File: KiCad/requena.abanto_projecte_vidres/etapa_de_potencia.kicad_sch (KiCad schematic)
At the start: 15 parts, among them U1 L298N, U2 TSR2-2450, U3 MCP6022, U4 LM1117DT-3.3

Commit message: millora_petjades
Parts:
- added FB1: FerriteBead, Inductor_SMD:L_0805_2012Metric, symbol Device:FerriteBead
- added J5: Conn_01x02, TerminalBlock:TerminalBlock_Xinya_XY308-2.54-2P_1x02_P2.54mm_Horizontal, symbol Connector_Generic:Conn_01x02
- added P1, P2: 282837-2, 282837-2:TE_282837-2, symbol 282837-2:282837-2
- C1, C5: footprint (none) -> Capacitor_SMD:C_0805_2012Metric
- C2, C6: footprint (none) -> Capacitor_SMD:C_1206_3216Metric
- C3, C4: footprint (none) -> Capacitor_THT:CP_Radial_D4.0mm_P1.50mm
- D1: footprint (none) -> Diode_THT:D_DO-41_SOD81_P12.70mm_Horizontal
- D2: footprint (none) -> Diode_THT:D_A-405_P2.54mm_Vertical_AnodeUp
- R1: value R_Shunt -> 5m; footprint (none) -> Resistor_SMD:R_1206_3216Metric
- R2: value R -> 1k; footprint (none) -> Resistor_SMD:R_1206_3216Metric
- R3: value R -> 300k; footprint (none) -> Resistor_SMD:R_1206_3216Metric
- U3: footprint (none) -> Package_SO:SOIC-8_3.9x4.9mm_P1.27mm
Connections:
- net +12V: now also J5.2 (Pin_2)
- net AN0: now also U3.6 (-); no longer R3.1, U3.1, U3.5 (+)
- net GND: now also FB1.2; no longer C1.2, C3.2, D2.2 (A), U2.2 (GND), U3.6 (-)
- net at U1.13 (OUT3): now also P2.1
- net at U1.14 (OUT4): now also P2.2
- net at U1.2 (OUT1): now also P1.1
- net at U1.3 (OUT2): now also P1.2
- new net: R3.1, U3.1, U3.5 (+)
- new net GNDPWR: C1.2, C3.2, D2.2 (A), FB1.1, J5.1 (Pin_1), U2.2 (GND)

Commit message: milora_esquema_i_layoutcomençat
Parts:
- P1, P2: footprint 282837-2:TE_282837-2 -> motor_connector:TE_282837-2
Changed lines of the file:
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@@
 			)
 		)
-		(property "Footprint" "282837-2:TE_282837-2"
+		(property "Footprint" "motor_connector:TE_282837-2"
 			(at 148.59 53.34 0)
 			(effects
@@
 			)
 		)
-		(property "Footprint" "282837-2:TE_282837-2"
+		(property "Footprint" "motor_connector:TE_282837-2"
 			(at 148.59 60.96 0)
 			(effects

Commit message: :(
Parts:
- C3: value 1uF -> 470uF
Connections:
- net +12V: no longer D1.2 (A)
- new net V_BAT: D1.2 (A)
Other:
- company: (none) -> AUTORS: ÀLEX REQUENA i ALFRED ABANTO
- title: (none) -> ETAPA DE POTÈNCIA
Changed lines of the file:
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@@
 	(generator_version "9.0")
 	(paper "A4")
+	(title_block
+		(title "ETAPA DE POTÈNCIA")
+		(company "AUTORS: ÀLEX REQUENA i ALFRED ABANTO")
+	)
 	(junction
 		(at 170.18 85.09)
@@
 	)
 	(junction
-		(at 62.23 127)
-		(diameter 0)
-		(color 0 0 0 0)
-	)
-	(junction
 		(at 189.23 143.51)
 		(diameter 0)
@@
 	(wire
 		(pts
-			(xy 62.23 127) (xy 62.23 138.43)
-		)
-		(stroke
-			(width 0)
-			(type default)
-		)
-	)
-	(wire
-		(pts
 			(xy 167.64 143.51) (xy 186.69 143.51)
 		)
@@
 	(wire
 		(pts
-			(xy 62.23 127) (xy 67.31 127)
-		)
-		(stroke
-			(width 0)
-			(type default)
-		)
-	)
-	(wire
-		(pts
 			(xy 208.28 99.06) (xy 208.28 101.6)
 		)
@@
 	(wire
 		(pts
+			(xy 64.77 127) (xy 67.31 127)
+		)
+		(stroke
+			(width 0)
+			(type default)
+		)
+	)
+	(wire
+		(pts
 			(xy 111.76 127) (xy 111.76 133.35)
-		)
-		(stroke
-			(width 0)
-			(type default)
-		)
-	)
-	(wire
-		(pts
-			(xy 62.23 123.19) (xy 62.23 127)
 		)
 		(stroke
@@
 	(global_label "V_BAT"
 		(shape input)
-		(at 62.23 138.43 270)
+		(at 64.77 127 180)
 		(fields_autoplaced yes)
 		(effects
@@
 		)
 		(property "Intersheetrefs" "${INTERSHEET_REFS}"
-			(at 62.23 146.7976 90)
+			(at 56.4024 127 0)
 			(effects
 				(font
@@
 	)
 	(symbol
-		(lib_id "power:+12V")
-		(at 62.23 123.19 0)
-		(unit 1)
-		(exclude_from_sim no)
-		(in_bom yes)
-		(on_board yes)
-		(dnp no)
-		(fields_autoplaced yes)
-		(property "Reference" "#PWR0109"
-			(at 62.23 127 0)
-			(effects
-				(font
-					(size 1.27 1.27)
-				)
-				(hide yes)
-			)
-		)
-		(property "Value" "+12V"
-			(at 62.23 118.11 0)
-			(effects
-				(font
-					(size 1.27 1.27)
-				)
-			)
-		)
-		(property "Footprint" ""
-			(at 62.23 123.19 0)
-			(effects
-				(font
-					(size 1.27 1.27)
-				)
-				(hide yes)
-			)
-		)
-		(property "Datasheet" ""
-			(at 62.23 123.19 0)
-			(effects
-				(font
-					(size 1.27 1.27)
-				)
-				(hide yes)
-			)
-		)
-		(property "Description" "Power symbol creates a global label with name \"+12V\""
-			(at 62.23 123.19 0)
-			(effects
-				(font
-					(size 1.27 1.27)
-				)
-				(hide yes)
-			)
-		)
-		(pin "1"
-		)
-		(instances
-			(project "etapa_de_potencia"
-				(path "/022df46b-4a1f-423b-84a0-dca974b893e8"
-					(reference "#PWR06")
-					(unit 1)
-				)
-			)
-			(project "requena.abanto_projecte_vidres"
-				(path "/4006572a-320d-4ed7-bf52-f860e1c069c6/0b0d2692-6fb2-4ddb-9a32-8981b2e43675"
-					(reference "#PWR0109")
-					(unit 1)
-				)
-			)
-		)
-	)
-	(symbol
 		(lib_id "Device:C")
 		(at 104.14 36.83 90)
@@
 			)
 		)
-		(property "Value" "1uF"
+		(property "Value" "470uF"
 			(at 115.57 137.5409 0)
 			(effects

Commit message: esquema acabat
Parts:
- P1, P2: footprint motor_connector:TE_282837-2 -> 282837-2:TE_282837-2
- R1: value 5m -> 50m; footprint Resistor_SMD:R_1206_3216Metric -> Resistor_SMD:R_Shunt_Vishay_WSK2512_6332Metric_T1.19mm
- R3: value 300k -> 12k
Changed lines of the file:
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@@
 			)
 		)
-		(property "Value" "300k"
+		(property "Value" "12k"
 			(at 163.83 92.71 90)
 			(effects
@@
 			)
 		)
-		(property "Footprint" "motor_connector:TE_282837-2"
+		(property "Footprint" "282837-2:TE_282837-2"
 			(at 148.59 53.34 0)
 			(effects
@@
 			)
 		)
-		(property "Footprint" "motor_connector:TE_282837-2"
+		(property "Footprint" "282837-2:TE_282837-2"
 			(at 148.59 60.96 0)
 			(effects
@@
 			)
 		)
-		(property "Value" "5m"
+		(property "Value" "50m"
 			(at 116.84 88.8999 0)
 			(effects
@@
 			)
 		)
-		(property "Footprint" "Resistor_SMD:R_1206_3216Metric"
+		(property "Footprint" "Resistor_SMD:R_Shunt_Vishay_WSK2512_6332Metric_T1.19mm"
 			(at 117.602 87.63 90)
 			(effects

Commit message: primera pcb
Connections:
- net +12V: no longer J5.2 (Pin_2)
- net V_BAT: now also J5.2 (Pin_2)
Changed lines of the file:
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@@
 	(wire
 		(pts
-			(xy 31.75 96.52) (xy 33.02 96.52)
+			(xy 31.75 96.52) (xy 35.56 96.52)
 		)
 		(stroke
@@
 		(property "Intersheetrefs" "${INTERSHEET_REFS}"
 			(at 208.28 73.3962 90)
+			(effects
+				(font
+					(size 1.27 1.27)
+				)
+				(justify left)
+				(hide yes)
+			)
+		)
+	)
+	(global_label "V_BAT"
+		(shape input)
+		(at 35.56 96.52 90)
+		(fields_autoplaced yes)
+		(effects
+			(font
+				(size 1.27 1.27)
+			)
+			(justify left)
+		)
+		(property "Intersheetrefs" "${INTERSHEET_REFS}"
+			(at 35.56 88.1524 90)
 			(effects
 				(font
@@
 					(unit 1)
 				)
-			)
-		)
-	)
-	(symbol
-		(lib_id "power:+12V")
-		(at 33.02 96.52 0)
-		(unit 1)
-		(exclude_from_sim no)
-		(in_bom yes)
-		(on_board yes)
-		(dnp no)
-		(fields_autoplaced yes)
-		(property "Reference" "#PWR02"
-			(at 33.02 100.33 0)
-			(effects
-				(font
-					(size 1.27 1.27)
-				)
-				(hide yes)
-			)
-		)
-		(property "Value" "+12V"
-			(at 33.02 91.44 0)
-			(effects
-				(font
-					(size 1.27 1.27)
-				)
-			)
-		)
-		(property "Footprint" ""
-			(at 33.02 96.52 0)
-			(effects
-				(font
-					(size 1.27 1.27)
-				)
-				(hide yes)
-			)
-		)
-		(property "Datasheet" ""
-			(at 33.02 96.52 0)
-			(effects
-				(font
-					(size 1.27 1.27)
-				)
-				(hide yes)
-			)
-		)
-		(property "Description" "Power symbol creates a global label with name \"+12V\""
-			(at 33.02 96.52 0)
-			(effects
-				(font
-					(size 1.27 1.27)
-				)
-				(hide yes)
-			)
-		)
-		(pin "1"
-		)
-		(instances
-			(project ""
-				(path "/4006572a-320d-4ed7-bf52-f860e1c069c6/0b0d2692-6fb2-4ddb-9a32-8981b2e43675"
-					(reference "#PWR02")
-					(unit 1)
-				)

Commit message: Avenç de placement
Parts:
- U4: footprint Package_TO_SOT_SMD:TO-252-3_TabPin2 -> Package_TO_SOT_SMD:TO-252-2
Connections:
- net +12V is gone; now on net V_BAT: U1.4 (Vs)
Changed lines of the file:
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@@
+		)
+	)
+	(global_label "V_BAT"
+		(shape input)
+		(at 121.92 35.56 90)
+		(fields_autoplaced yes)
+		(effects
+			(font
+				(size 1.27 1.27)
+			)
+			(justify left)
+		)
+		(property "Intersheetrefs" "${INTERSHEET_REFS}"
+			(at 121.92 27.1924 90)
+			(effects
+				(font
+					(size 1.27 1.27)
+				)
+				(justify left)
+				(hide yes)
+			)
 		)
 	)
@@
 			)
 		)
-		(property "Footprint" "Package_TO_SOT_SMD:TO-252-3_TabPin2"
+		(property "Footprint" "Package_TO_SOT_SMD:TO-252-2"
 			(at 167.64 127 0)
 			(effects
@@
 					(unit 1)
 				)
-			)
-		)
-	)
-	(symbol
-		(lib_id "power:+12V")
-		(at 121.92 35.56 0)
-		(unit 1)
-		(exclude_from_sim no)
-		(in_bom yes)
-		(on_board yes)
-		(dnp no)
-		(fields_autoplaced yes)
-		(property "Reference" "#PWR0101"
-			(at 121.92 39.37 0)
-			(effects
-				(font
-					(size 1.27 1.27)
-				)
-				(hide yes)
-			)
-		)
-		(property "Value" "+12V"
-			(at 121.92 30.48 0)
-			(effects
-				(font
-					(size 1.27 1.27)
-				)
-			)
-		)
-		(property "Footprint" ""
-			(at 121.92 35.56 0)
-			(effects
-				(font
-					(size 1.27 1.27)
-				)
-				(hide yes)
-			)
-		)
-		(property "Datasheet" ""
-			(at 121.92 35.56 0)
-			(effects
-				(font
-					(size 1.27 1.27)
-				)
-				(hide yes)
-			)
-		)
-		(property "Description" "Power symbol creates a global label with name \"+12V\""
-			(at 121.92 35.56 0)
-			(effects
-				(font
-					(size 1.27 1.27)
-				)
-				(hide yes)
-			)
-		)
-		(pin "1"
-		)
-		(instances
-			(project ""
-				(path "/022df46b-4a1f-423b-84a0-dca974b893e8"
-					(reference "#PWR01")
-					(unit 1)
-				)
-			)
-			(project "requena.abanto_projecte_vidres"
-				(path "/4006572a-320d-4ed7-bf52-f860e1c069c6/0b0d2692-6fb2-4ddb-9a32-8981b2e43675"
-					(reference "#PWR0101")
-					(unit 1)
-				)

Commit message: placement pcb
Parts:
- added C22: 10uF, Capacitor_THT:CP_Radial_D4.0mm_P1.50mm, symbol Device:C_Polarized
- added C23: 100nF, Capacitor_SMD:C_0805_2012Metric, symbol Device:C
- added C24: 47uF, Capacitor_THT:CP_Radial_D4.0mm_P1.50mm, symbol Device:C_Polarized
- C4: value 1uF -> 10uF
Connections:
- net GND: now also C22.2
- net GNDPWR: now also C23.2, C24.2
- net V_OUT_DCDC: now also C22.1, C23.1, C24.1
- net V_BAT': now reaches C1.1, C3.1, D1.1 (K), D2.1 (K), U2.1 (Vin)
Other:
- moved on the sheet: C4, C5, J5, U4

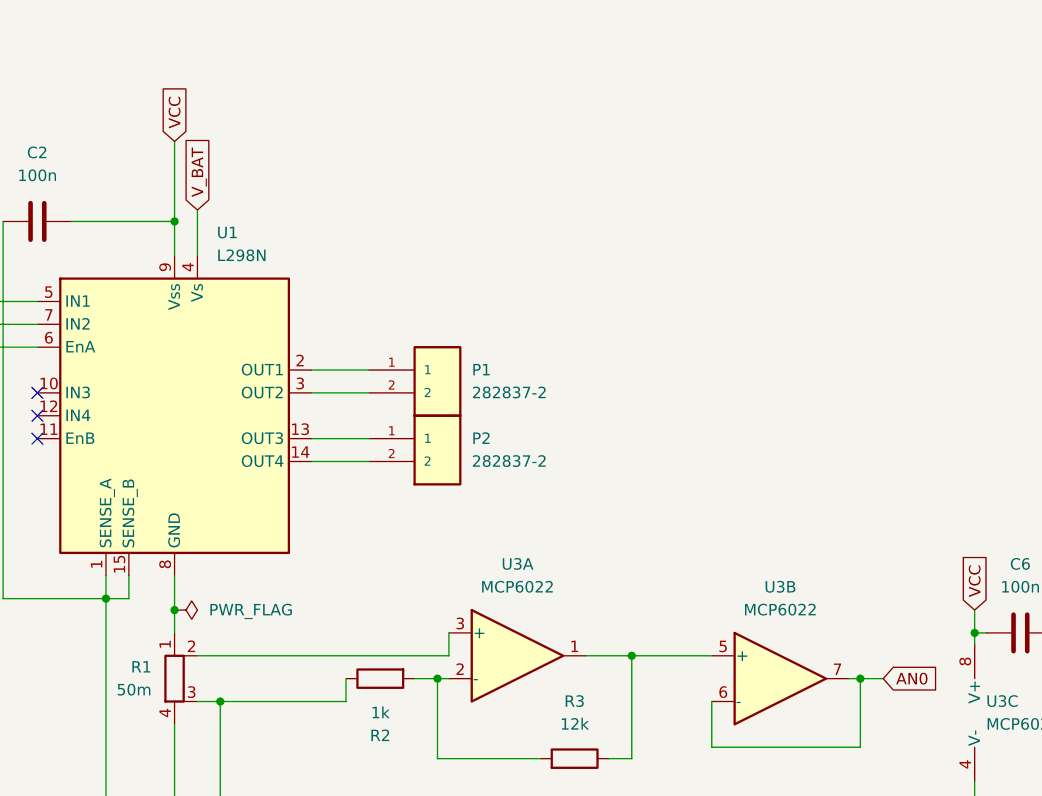
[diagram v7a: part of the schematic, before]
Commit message: ficat diodes de proteccion driver
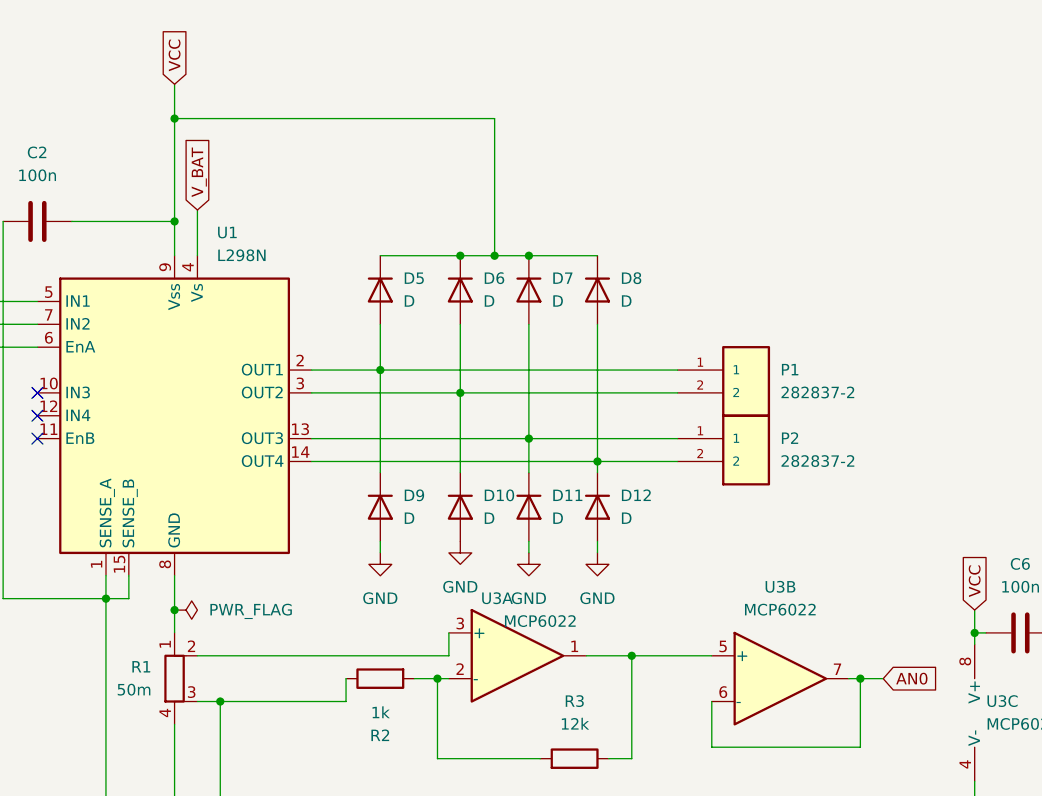
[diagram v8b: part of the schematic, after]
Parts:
- added D10, D11, D12, D5, D6, D7, D8, D9: D, Diode_THT:D_DO-201AD_P15.24mm_Horizontal, symbol Device:D
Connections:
- net GND: now also D10.2 (A), D11.2 (A), D12.2 (A), D9.2 (A)
- net VCC: now also D5.1 (K), D6.1 (K), D7.1 (K), D8.1 (K)
- net at P1.1, U1.2 (OUT1): now also D5.2 (A), D9.1 (K)
- net at P1.2, U1.3 (OUT2): now also D10.1 (K), D6.2 (A)
- net at P2.1, U1.13 (OUT3): now also D11.1 (K), D7.2 (A)
- net at P2.2, U1.14 (OUT4): now also D12.1 (K), D8.2 (A)
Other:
- moved on the sheet: P1, P2
